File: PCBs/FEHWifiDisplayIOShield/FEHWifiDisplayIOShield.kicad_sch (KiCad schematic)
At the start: 17 parts, among them J1 Conn_01x16_Socket, J2 Conn_02x04_Counter_Clockwise, J3 JST_2MM_MALE, SW1 SW_MEC_5G, SW2 SW_MEC_5G, SW3 SW_MEC_5G, SW4 SW_MEC_5G

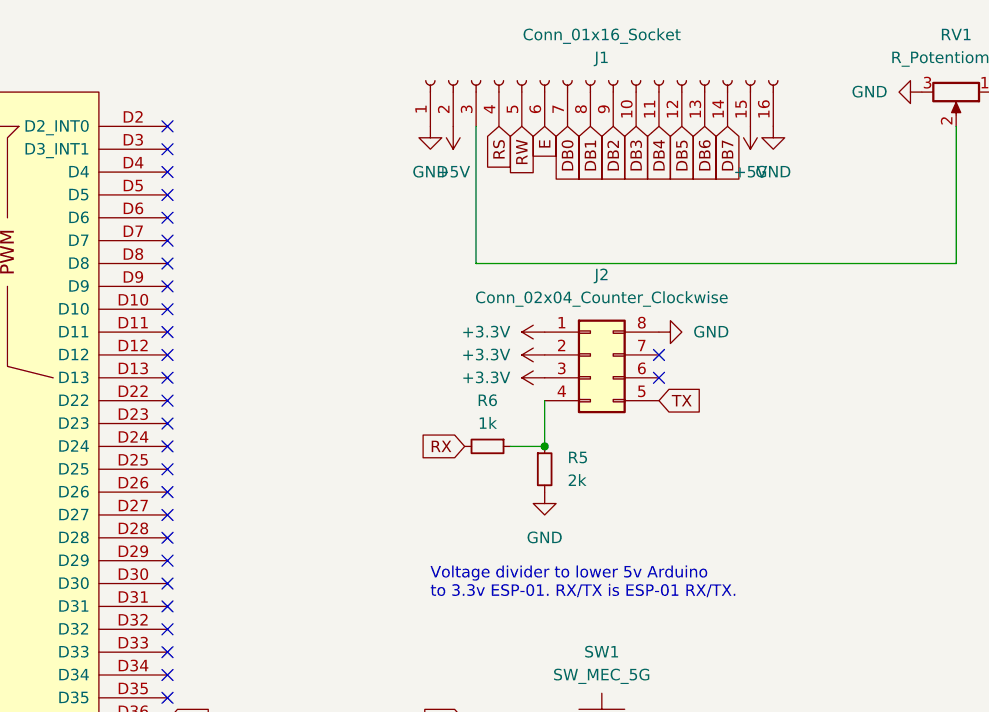
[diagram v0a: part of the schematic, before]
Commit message: Added interrupt connection and fixed tx/rx error
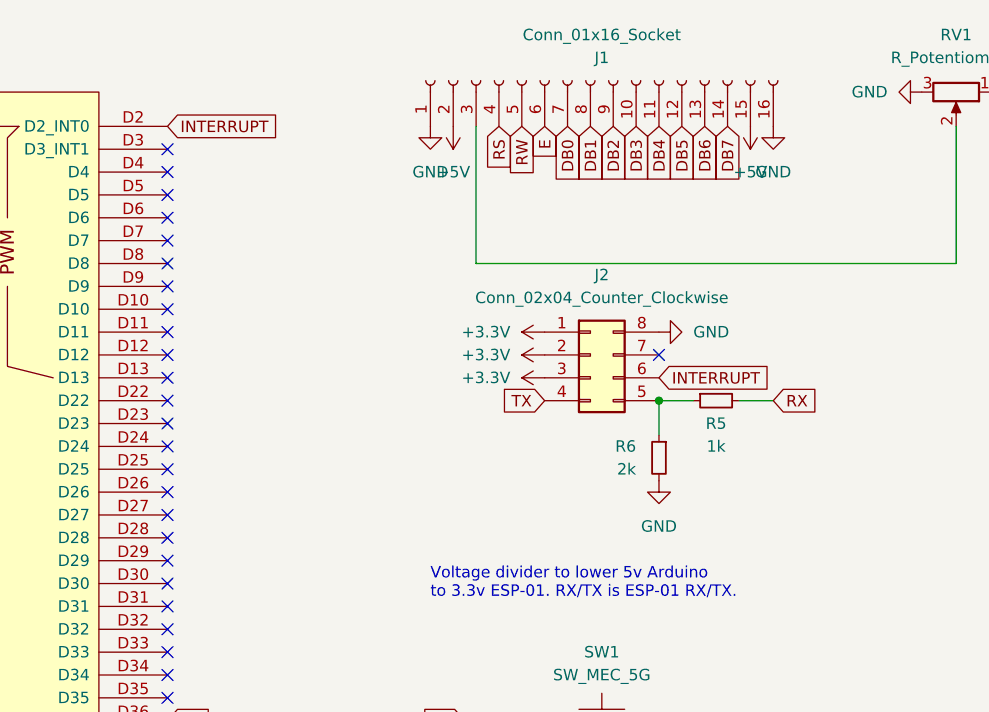
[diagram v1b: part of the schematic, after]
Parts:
- R5: value 2k -> 1k
- R6: value 1k -> 2k
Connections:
- net GND: now also R6.2; no longer R5.2
- net RX: now also R5.2; no longer R6.2
- net TX: now also J2.4 (Pin_4); no longer J2.5 (Pin_5)
- net at R5.1, R6.1: now also J2.5 (Pin_5); no longer J2.4 (Pin_4)
- net INTERRUPT: now reaches A1.D2 (D2_INT0)
- net INTERRUPT: now also J2.6 (Pin_6)
- no-connect marks 74 -> 72
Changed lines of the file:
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@@
   (junction (at 127 106.68) (diameter 0) (color 0 0 0 0)
   )
+  (junction (at 142.24 60.96) (diameter 0) (color 0 0 0 0)
+  )
   (junction (at 127 116.84) (diameter 0) (color 0 0 0 0)
   )
@@
   )
   (junction (at 127 96.52) (diameter 0) (color 0 0 0 0)
-  )
-  (junction (at 129.54 66.04) (diameter 0) (color 0 0 0 0)
   )
   (junction (at 140.97 116.84) (diameter 0) (color 0 0 0 0)
@@
   (no_connect (at 87.63 66.04))
   (no_connect (at 21.59 40.64))
-  (no_connect (at 87.63 30.48))
   (no_connect (at 58.42 162.56))
   (no_connect (at 53.34 19.05))
@@
   (no_connect (at 87.63 60.96))
   (no_connect (at 58.42 19.05))
-  (no_connect (at 142.24 58.42))
   (no_connect (at 21.59 45.72))
   (no_connect (at 87.63 38.1))
@@
     (stroke (width 0) (type default))
   )
-  (wire (pts (xy 129.54 60.96) (xy 129.54 66.04))
-    (stroke (width 0) (type default))
-  )
   (wire (pts (xy 52.07 172.72) (xy 52.07 175.26))
     (stroke (width 0) (type default))
@@
     (stroke (width 0) (type default))
   )
-  (wire (pts (xy 125.73 66.04) (xy 129.54 66.04))
+  (wire (pts (xy 142.24 64.77) (xy 142.24 60.96))
     (stroke (width 0) (type default))
   )
@@
     (stroke (width 0) (type default))
   )
+  (wire (pts (xy 151.13 60.96) (xy 154.94 60.96))
+    (stroke (width 0) (type default))
+  )
   (wire (pts (xy 121.92 30.48) (xy 121.92 45.72))
     (stroke (width 0) (type default))
@@
   )
   (wire (pts (xy 127 116.84) (xy 130.81 116.84))
+    (stroke (width 0) (type default))
+  )
+  (wire (pts (xy 146.05 60.96) (xy 142.24 60.96))
     (stroke (width 0) (type default))
   )
@@
     (effects (font (size 1.27 1.27)) (justify left bottom))
   )
+  (global_label "INTERRUPT" (shape input) (at 87.63 30.48 0) (fields_autoplaced)
+    (effects (font (size 1.27 1.27)) (justify left))
+    (property "Intersheetrefs" "${INTERSHEET_REFS}" (at 100.6958 30.48 0)
+      (effects (font (size 1.27 1.27)) (justify left) hide)
+    )
+  )
   (global_label "RS" (shape input) (at 87.63 96.52 0) (fields_autoplaced)
     (effects (font (size 1.27 1.27)) (justify left))
@@
     )
   )
-  (global_label "TX" (shape input) (at 142.24 60.96 0) (fields_autoplaced)
-    (effects (font (size 1.27 1.27)) (justify left))
-    (property "Intersheetrefs" "${INTERSHEET_REFS}" (at 147.3229 60.96 0)
-      (effects (font (size 1.27 1.27)) (justify left) hide)
+  (global_label "TX" (shape input) (at 129.54 60.96 180) (fields_autoplaced)
+    (effects (font (size 1.27 1.27)) (justify right))
+    (property "Intersheetrefs" "${INTERSHEET_REFS}" (at 124.4571 60.96 0)
+      (effects (font (size 1.27 1.27)) (justify right) hide)
     )
   )
@@
     )
   )
+  (global_label "RX" (shape input) (at 154.94 60.96 0) (fields_autoplaced)
+    (effects (font (size 1.27 1.27)) (justify left))
+    (property "Intersheetrefs" "${INTERSHEET_REFS}" (at 160.3253 60.96 0)
+      (effects (font (size 1.27 1.27)) (justify left) hide)
+    )
+  )
   (global_label "RX" (shape input) (at 21.59 38.1 180) (fields_autoplaced)
     (effects (font (size 1.27 1.27)) (justify right))
@@
     )
   )
+  (global_label "INTERRUPT" (shape input) (at 142.24 58.42 0) (fields_autoplaced)
+    (effects (font (size 1.27 1.27)) (justify left))
+    (property "Intersheetrefs" "${INTERSHEET_REFS}" (at 155.3058 58.42 0)
+      (effects (font (size 1.27 1.27)) (justify left) hide)
+    )
+  )
   (global_label "47" (shape input) (at 120.65 96.52 180) (fields_autoplaced)
     (effects (font (size 1.27 1.27)) (justify right))
     (property "Intersheetrefs" "${INTERSHEET_REFS}" (at 115.3252 96.52 0)
-      (effects (font (size 1.27 1.27)) (justify right) hide)
-    )
-  )
-  (global_label "RX" (shape input) (at 120.65 66.04 180) (fields_autoplaced)
-    (effects (font (size 1.27 1.27)) (justify right))
-    (property "Intersheetrefs" "${INTERSHEET_REFS}" (at 115.2647 66.04 0)
       (effects (font (size 1.27 1.27)) (justify right) hide)
     )
@@
         (path "/9d3c453f-c215-40bd-a6b9-e71fa247cacf"
           (reference "J3") (unit 1)
-        )
-      )
-    )
-  )
-  (symbol (lib_id "Device:R_Small") (at 129.54 68.58 0) (unit 1)
-    (in_bom yes) (on_board yes) (dnp no) (fields_autoplaced)
-    (property "Reference" "R5" (at 132.08 67.31 0)
-      (effects (font (size 1.27 1.27)) (justify left))
-    )
-    (property "Value" "2k" (at 132.08 69.85 0)
-      (effects (font (size 1.27 1.27)) (justify left))
-    )
-    (property "Footprint" "" (at 129.54 68.58 0)
-      (effects (font (size 1.27 1.27)) hide)
-    )
-    (property "Datasheet" "~" (at 129.54 68.58 0)
-      (effects (font (size 1.27 1.27)) hide)
-    )
-    (pin "1")
-    (pin "2")
-    (instances
-      (project "FEHWifiDisplayIOShield"
-        (path "/9d3c453f-c215-40bd-a6b9-e71fa247cacf"
-          (reference "R5") (unit 1)
         )
       )
@@
     )
   )
-  (symbol (lib_id "power:GND") (at 129.54 71.12 0) (unit 1)
-    (in_bom yes) (on_board yes) (dnp no) (fields_autoplaced)
-    (property "Reference" "#PWR020" (at 129.54 77.47 0)
-      (effects (font (size 1.27 1.27)) hide)
-    )
-    (property "Value" "GND" (at 129.54 76.2 0)
-      (effects (font (size 1.27 1.27)))
-    )
-    (property "Footprint" "" (at 129.54 71.12 0)
-      (effects (font (size 1.27 1.27)) hide)
-    )
-    (property "Datasheet" "" (at 129.54 71.12 0)
-      (effects (font (size 1.27 1.27)) hide)
-    )
-    (pin "1")
-    (instances
-      (project "FEHWifiDisplayIOShield"
-        (path "/9d3c453f-c215-40bd-a6b9-e71fa247cacf"
-          (reference "#PWR020") (unit 1)
-        )
-      )
-    )
-  )
   (symbol (lib_id "Device:R_Small") (at 127 99.06 0) (unit 1)
     (in_bom yes) (on_board yes) (dnp no) (fields_autoplaced)
@@
         (path "/9d3c453f-c215-40bd-a6b9-e71fa247cacf"
           (reference "C1") (unit 1)
+        )
+      )
+    )
+  )
+  (symbol (lib_id "power:GND") (at 142.24 69.85 0) (mirror y) (unit 1)
+    (in_bom yes) (on_board yes) (dnp no) (fields_autoplaced)
+    (property "Reference" "#PWR020" (at 142.24 76.2 0)
+      (effects (font (size 1.27 1.27)) hide)
+    )
+    (property "Value" "GND" (at 142.24 74.93 0)
+      (effects (font (size 1.27 1.27)))
+    )
+    (property "Footprint" "" (at 142.24 69.85 0)
+      (effects (font (size 1.27 1.27)) hide)
+    )
+    (property "Datasheet" "" (at 142.24 69.85 0)
+      (effects (font (size 1.27 1.27)) hide)
+    )
+    (pin "1")
+    (instances
+      (project "FEHWifiDisplayIOShield"
+        (path "/9d3c453f-c215-40bd-a6b9-e71fa247cacf"
+          (reference "#PWR020") (unit 1)
         )
       )
@@
     )
   )
-  (symbol (lib_id "Device:R_Small") (at 123.19 66.04 270) (unit 1)
-    (in_bom yes) (on_board yes) (dnp no) (fields_autoplaced)
-    (property "Reference" "R6" (at 123.19 60.96 90)
-      (effects (font (size 1.27 1.27)))
-    )
-    (property "Value" "1k" (at 123.19 63.5 90)
-      (effects (font (size 1.27 1.27)))
-    )
-    (property "Footprint" "" (at 123.19 66.04 0)
-      (effects (font (size 1.27 1.27)) hide)
-    )
-    (property "Datasheet" "~" (at 123.19 66.04 0)
+  (symbol (lib_id "Device:R_Small") (at 148.59 60.96 90) (mirror x) (unit 1)
+    (in_bom yes) (on_board yes) (dnp no)
+    (property "Reference" "R5" (at 148.59 63.5 90)
+      (effects (font (size 1.27 1.27)))
+    )
+    (property "Value" "1k" (at 148.59 66.04 90)
+      (effects (font (size 1.27 1.27)))
+    )
+    (property "Footprint" "" (at 148.59 60.96 0)
+      (effects (font (size 1.27 1.27)) hide)
+    )
+    (property "Datasheet" "~" (at 148.59 60.96 0)
       (effects (font (size 1.27 1.27)) hide)
     )
@@
       (project "FEHWifiDisplayIOShield"
         (path "/9d3c453f-c215-40bd-a6b9-e71fa247cacf"
-          (reference "R6") (unit 1)
+          (reference "R5") (unit 1)
         )
       )
@@
         )
       )
+    )
+  )
+  (symbol (lib_id "Device:R_Small") (at 142.24 67.31 0) (mirror y) (unit 1)
+    (in_bom yes) (on_board yes) (dnp no)
+    (property "Reference" "R6" (at 139.7 66.04 0)
+      (effects (font (size 1.27 1.27)) (justify left))
+    )
+    (property "Value" "2k" (at 139.7 68.58 0)
+      (effects (font (size 1.27 1.27)) (justify left))
+    )
+    (property "Footprint" "" (at 142.24 67.31 0)
+      (effects (font (size 1.27 1.27)) hide)
+    )
+    (property "Datasheet" "~" (at 142.24 67.31 0)
+      (effects (font (size 1.27 1.27)) hide)
+    )
+    (pin "1")
+    (pin "2")
+    (instances
+      (project "FEHWifiDisplayIOShield"
+        (path "/9d3c453f-c215-40bd-a6b9-e71fa247cacf"
+          (reference "R6") (unit 1)
+        )
+      )

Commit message: Added pullodown resistor on interrupt pin
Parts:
- added R7: 10k, symbol Device:R_Small
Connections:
- net GND: now also R7.1
- net INTERRUPT: now also R7.2
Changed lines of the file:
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@@
   (junction (at 142.24 60.96) (diameter 0) (color 0 0 0 0)
+  )
+  (junction (at 92.71 30.48) (diameter 0) (color 0 0 0 0)
   )
   (junction (at 127 116.84) (diameter 0) (color 0 0 0 0)
@@
     (stroke (width 0) (type default))
   )
+  (wire (pts (xy 97.79 30.48) (xy 92.71 30.48))
+    (stroke (width 0) (type default))
+  )
   (wire (pts (xy 55.88 170.18) (xy 55.88 172.72))
     (stroke (width 0) (type default))
@@
     (stroke (width 0) (type default))
   )
+  (wire (pts (xy 92.71 30.48) (xy 87.63 30.48))
+    (stroke (width 0) (type default))
+  )
+  (wire (pts (xy 92.71 21.59) (xy 92.71 22.86))
+    (stroke (width 0) (type default))
+  )
   (wire (pts (xy 120.65 106.68) (xy 127 106.68))
+    (stroke (width 0) (type default))
+  )
+  (wire (pts (xy 92.71 27.94) (xy 92.71 30.48))
     (stroke (width 0) (type default))
   )
@@
     (effects (font (size 1.27 1.27)) (justify left bottom))
   )
-  (global_label "INTERRUPT" (shape input) (at 87.63 30.48 0) (fields_autoplaced)
-    (effects (font (size 1.27 1.27)) (justify left))
-    (property "Intersheetrefs" "${INTERSHEET_REFS}" (at 100.6958 30.48 0)
+  (global_label "INTERRUPT" (shape input) (at 97.79 30.48 0) (fields_autoplaced)
+    (effects (font (size 1.27 1.27)) (justify left))
+    (property "Intersheetrefs" "${INTERSHEET_REFS}" (at 110.8558 30.48 0)
       (effects (font (size 1.27 1.27)) (justify left) hide)
     )
@@
     (property "Intersheetrefs" "${INTERSHEET_REFS}" (at 92.9548 129.54 0)
       (effects (font (size 1.27 1.27)) (justify left) hide)
+    )
+  )
+  (symbol (lib_id "Device:R_Small") (at 92.71 25.4 0) (unit 1)
+    (in_bom yes) (on_board yes) (dnp no) (fields_autoplaced)
+    (property "Reference" "R7" (at 95.25 24.13 0)
+      (effects (font (size 1.27 1.27)) (justify left))
+    )
+    (property "Value" "10k" (at 95.25 26.67 0)
+      (effects (font (size 1.27 1.27)) (justify left))
+    )
+    (property "Footprint" "" (at 92.71 25.4 0)
+      (effects (font (size 1.27 1.27)) hide)
+    )
+    (property "Datasheet" "~" (at 92.71 25.4 0)
+      (effects (font (size 1.27 1.27)) hide)
+    )
+    (pin "1")
+    (pin "2")
+    (instances
+      (project "FEHWifiDisplayIOShield"
+        (path "/9d3c453f-c215-40bd-a6b9-e71fa247cacf"
+          (reference "R7") (unit 1)
+        )
+      )
     )
   )
@@
         )
       )
+    )
+  )
+  (symbol (lib_id "power:GND") (at 92.71 21.59 180) (unit 1)
+    (in_bom yes) (on_board yes) (dnp no) (fields_autoplaced)
+    (property "Reference" "#PWR027" (at 92.71 15.24 0)
+      (effects (font (size 1.27 1.27)) hide)
+    )
+    (property "Value" "GND" (at 92.71 16.51 0)
+      (effects (font (size 1.27 1.27)))
+    )
+    (property "Footprint" "" (at 92.71 21.59 0)
+      (effects (font (size 1.27 1.27)) hide)
+    )
+    (property "Datasheet" "" (at 92.71 21.59 0)
+      (effects (font (size 1.27 1.27)) hide)
+    )
+    (pin "1")
+    (instances
+      (project "FEHWifiDisplayIOShield"
+        (path "/9d3c453f-c215-40bd-a6b9-e71fa247cacf"
+          (reference "#PWR027") (unit 1)
+        )
+      )
